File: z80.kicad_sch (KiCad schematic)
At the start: 41 parts, among them IC4 Z80CPU, IC5 LC3664, IC901 TL972

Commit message: more component parts updated
Full in the * as PAL versions.
Added MPN for PCBWAY
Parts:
- C602: MPN (none) -> VJ0805Y104JXJMT
- C901, C902: MPN (none) -> VJ0805V106ZXQTW1BC
- C903: MPN (none) -> VJ0805Y223JXJPW1BC
- C903, C904, C905, C906, C907, C908: MPN (none) -> VJ0805Y105KXJTW1BC
- C910, C911: MPN (none) -> VJ0805A151FXJCW1BC
- IC901: MPN (none) -> TL972IDR
- R901, R902: MPN (none) -> CRCW0805100KFKEA
- R903, R904, R905, R906, R907, R908: MPN (none) -> CRCW0805210KFKEA
- R909, R910: MPN (none) -> CRCW080575R0FKEAHP
- R910, R911: MPN (none) -> RCS0805300KFKEA
- R911: MPN (none) -> CRCW08052K20JNEA
- R912, R913: MPN (none) -> CRCW0805330RFKEA
- R914, R915: MPN (none) -> CRCW080510K0FKEA
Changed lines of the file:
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@@
+      (effects (font (size 1.27 1.27)) hide)
+    )
+    (property "MPN" "VJ0805Y105KXJTW1BC" (at 115.57 231.775 0)
       (effects (font (size 1.27 1.27)) hide)
     )
@@
       (effects (font (size 1.27 1.27)) hide)
     )
+    (property "MPN" "VJ0805A151FXJCW1BC" (at 189.865 175.26 0)
+      (effects (font (size 1.27 1.27)) hide)
+    )
     (pin "1")
     (pin "2")
@@
       (effects (font (size 1.27 1.27)) hide)
     )
+    (property "MPN" "VJ0805V106ZXQTW1BC" (at 115.57 253.365 0)
+      (effects (font (size 1.27 1.27)) hide)
+    )
     (pin "1")
     (pin "2")
@@
     )
     (property "LCSC Part #" "C2080690" (at 145.415 186.055 0)
+      (effects (font (size 1.27 1.27)) hide)
+    )
+    (property "MPN" "CRCW0805210KFKEA" (at 145.415 186.055 0)
       (effects (font (size 1.27 1.27)) hide)
     )
@@
     )
     (property "LCSC Part #" "" (at 221.615 234.315 0)
+      (effects (font (size 1.27 1.27)) hide)
+    )
+    (property "MPN" "" (at 221.615 234.315 0)
       (effects (font (size 1.27 1.27)) hide)
     )
@@
     )
     (property "LCSC Part #" "C46127" (at 189.865 234.315 0)
+      (effects (font (size 1.27 1.27)) hide)
+    )
+    (property "MPN" "TL972IDR" (at 189.865 234.315 0)
       (effects (font (size 1.27 1.27)) hide)
     )
@@
       (effects (font (size 1.27 1.27)) hide)
     )
+    (property "MPN" "CRCW0805210KFKEA" (at 145.415 212.09 0)
+      (effects (font (size 1.27 1.27)) hide)
+    )
     (pin "1")
     (pin "2")
@@
       (effects (font (size 1.27 1.27)) hide)
     )
+    (property "MPN" "CRCW080575R0FKEAHP" (at 101.6 238.76 0)
+      (effects (font (size 1.27 1.27)) hide)
+    )
     (pin "1")
     (pin "2")
@@
     )
     (property "LCSC Part #" "C1850591" (at 115.57 242.57 0)
+      (effects (font (size 1.27 1.27)) hide)
+    )
+    (property "MPN" "VJ0805Y105KXJTW1BC" (at 115.57 242.57 0)
       (effects (font (size 1.27 1.27)) hide)
     )
@@
       (effects (font (size 1.27 1.27)) hide)
     )
+    (property "MPN" "CRCW0805210KFKEA" (at 145.415 231.775 0)
+      (effects (font (size 1.27 1.27)) hide)
+    )
     (pin "1")
     (pin "2")
@@
     )
     (property "LCSC Part #" "C2080690" (at 145.415 242.57 0)
+      (effects (font (size 1.27 1.27)) hide)
+    )
+    (property "MPN" "CRCW0805210KFKEA" (at 145.415 242.57 0)
       (effects (font (size 1.27 1.27)) hide)
     )
@@
       (effects (font (size 1.27 1.27)) hide)
     )
+    (property "MPN" "VJ0805Y104JXJMT" (at 262.89 238.76 0)
+      (effects (font (size 1.27 1.27)) hide)
+    )
     (pin "1")
     (pin "2")
@@
     )
     (property "LCSC Part #" "C844935" (at 145.415 175.26 0)
+      (effects (font (size 1.27 1.27)) hide)
+    )
+    (property "MPN" "CRCW0805100KFKEA" (at 145.415 175.26 0)
       (effects (font (size 1.27 1.27)) hide)
     )
@@
       (effects (font (size 1.27 1.27)) hide)
     )
+    (property "MPN" "CRCW080575R0FKEAHP" (at 52.07 175.26 0)
+      (effects (font (size 1.27 1.27)) hide)
+    )
     (pin "1")
     (pin "2")
@@
     )
     (property "LCSC Part #" "C46127" (at 189.865 194.31 0)
+      (effects (font (size 1.27 1.27)) hide)
+    )
+    (property "MPN" "TL972IDR" (at 189.865 194.31 0)
       (effects (font (size 1.27 1.27)) hide)
     )
@@
       (effects (font (size 1.27 1.27)) hide)
     )
+    (property "MPN" "" (at 80.772 33.782 0)
+      (effects (font (size 1.27 1.27)) hide)
+    )
     (pin "1")
     (pin "2")
@@
       (effects (font (size 1.27 1.27)) hide)
     )
+    (property "MPN" "CRCW0805210KFKEA" (at 145.415 218.44 0)
+      (effects (font (size 1.27 1.27)) hide)
+    )
     (pin "1")
     (pin "2")
@@
       (effects (font (size 1.27 1.27)) hide)
     )
+    (property "MPN" "VJ0805Y223JXJPW1BC" (at 167.64 33.655 0)
+      (effects (font (size 1.27 1.27)) hide)
+    )
     (pin "1")
     (pin "2")
@@
       (effects (font (size 1.27 1.27)) hide)
     )
+    (property "MPN" "VJ0805V106ZXQTW1BC" (at 115.57 175.26 0)
+      (effects (font (size 1.27 1.27)) hide)
+    )
     (pin "1")
     (pin "2")
@@
       (effects (font (size 1.27 1.27)) hide)
     )
+    (property "MPN" "CRCW080510K0FKEA" (at 162.56 222.25 0)
+      (effects (font (size 1.27 1.27)) hide)
+    )
     (pin "1")
     (pin "2")
@@
       (effects (font (size 1.27 1.27)) hide)
     )
+    (property "MPN" "VJ0805Y105KXJTW1BC" (at 115.57 186.055 0)
+      (effects (font (size 1.27 1.27)) hide)
+    )
     (pin "1")
     (pin "2")
@@
       (effects (font (size 1.27 1.27)) hide)
     )
+    (property "MPN" "VJ0805A151FXJCW1BC" (at 189.865 253.365 0)
+      (effects (font (size 1.27 1.27)) hide)
+    )
     (pin "1")
     (pin "2")
@@
       (effects (font (size 1.27 1.27)) hide)
     )
+    (property "MPN" "RCS0805300KFKEA" (at 189.865 186.055 0)
+      (effects (font (size 1.27 1.27)) hide)
+    )
     (pin "1")
     (pin "2")
@@
       (effects (font (size 1.27 1.27)) hide)
     )
+    (property "MPN" "CRCW080510K0FKEA" (at 162.56 208.28 0)
+      (effects (font (size 1.27 1.27)) hide)
+    )
     (pin "1")
     (pin "2")
@@
     )
     (property "LCSC Part #" "C313959" (at 102.235 203.835 0)
+      (effects (font (size 1.27 1.27)) hide)
+    )
+    (property "MPN" "CRCW080575R0FKEAHP" (at 102.235 203.835 0)
       (effects (font (size 1.27 1.27)) hide)
     )
@@
     )
     (property "LCSC Part #" "" (at 221.615 194.31 0)
+      (effects (font (size 1.27 1.27)) hide)
+    )
+    (property "MPN" "" (at 221.615 194.31 0)
       (effects (font (size 1.27 1.27)) hide)
     )
@@
       (effects (font (size 1.27 1.27)) hide)
     )
+    (property "MPN" "" (at 170.18 222.25 0)
+      (effects (font (size 1.27 1.27)) hide)
+    )
     (pin "1")
     (pin "2")
@@
       (effects (font (size 1.27 1.27)) hide)
     )
+    (property "MPN" "VJ0805Y105KXJTW1BC" (at 129.54 218.44 0)
+      (effects (font (size 1.27 1.27)) hide)
+    )
     (pin "1")
     (pin "2")
@@
       (effects (font (size 1.27 1.27)) hide)
     )
+    (property "MPN" "CRCW0805210KFKEA" (at 145.415 196.85 0)
+      (effects (font (size 1.27 1.27)) hide)
+    )
     (pin "1")
     (pin "2")
@@
     )
     (property "LCSC Part #" "C3008897" (at 102.235 222.25 0)
+      (effects (font (size 1.27 1.27)) hide)
+    )
+    (property "MPN" "CRCW08052K20JNEA" (at 102.235 222.25 0)
       (effects (font (size 1.27 1.27)) hide)
     )
@@
       (effects (font (size 1.27 1.27)) hide)
     )
+    (property "MPN" "" (at 275.59 238.76 0)
+      (effects (font (size 1.27 1.27)) hide)
+    )
     (pin "1")
     (pin "2")
@@
       (effects (font (size 1.27 1.27)) hide)
     )
+    (property "MPN" "VJ0805Y223JXJPW1BC" (at 93.472 33.782 0)
+      (effects (font (size 1.27 1.27)) hide)
+    )
     (pin "1")
     (pin "2")
@@
     )
     (property "LCSC Part #" "C844935" (at 145.415 253.365 0)
+      (effects (font (size 1.27 1.27)) hide)
+    )
+    (property "MPN" "CRCW0805100KFKEA" (at 145.415 253.365 0)
       (effects (font (size 1.27 1.27)) hide)
     )
@@
     )
     (property "LCSC Part #" "C844839" (at 210.82 234.315 0)
+      (effects (font (size 1.27 1.27)) hide)
+    )
+    (property "MPN" "CRCW0805330RFKEA" (at 210.82 234.315 0)
       (effects (font (size 1.27 1.27)) hide)
     )
@@
     )
     (property "LCSC Part #" "" (at 74.93 83.185 0)
+      (effects (font (size 1.27 1.27)) hide)
+    )
+    (property "MPN" "" (at 74.93 83.185 0)
       (effects (font (size 1.27 1.27)) hide)
     )
@@
       (effects (font (size 1.27 1.27)) hide)
     )
+    (property "MPN" "TL972IDR" (at 290.195 239.395 0)
+      (effects (font (size 1.27 1.27)) hide)
+    )
     (pin "1")
     (pin "2")
@@
       (effects (font (size 1.27 1.27)) hide)
     )
+    (property "MPN" "RCS0805300KFKEA" (at 189.865 242.57 0)
+      (effects (font (size 1.27 1.27)) hide)
+    )
     (pin "1")
     (pin "2")
@@
     )
     (property "LCSC Part #" "C1850591" (at 129.54 212.09 0)
+      (effects (font (size 1.27 1.27)) hide)
+    )
+    (property "MPN" "VJ0805Y105KXJTW1BC" (at 129.54 212.09 0)
       (effects (font (size 1.27 1.27)) hide)
     )
@@
     )
     (property "LCSC Part #" "C844839" (at 210.82 194.31 0)
+      (effects (font (size 1.27 1.27)) hide)
+    )
+    (property "MPN" "CRCW0805330RFKEA" (at 210.82 194.31 0)
       (effects (font (size 1.27 1.27)) hide)
     )
@@
     )
     (property "LCSC Part #" "" (at 158.75 80.645 0)
+      (effects (font (size 1.27 1.27)) hide)
+    )
+    (property "MPN" "" (at 158.75 80.645 0)
       (effects (font (size 1.27 1.27)) hide)
     )
@@
       (effects (font (size 1.27 1.27)) hide)
     )
+    (property "MPN" "CRCW080575R0FKEAHP" (at 52.07 191.135 0)
+      (effects (font (size 1.27 1.27)) hide)
+    )
     (pin "1")
     (pin "2")
@@
     )
     (property "LCSC Part #" "" (at 219.71 109.22 0)
+      (effects (font (size 1.27 1.27)) hide)
+    )
+    (property "MPN" "" (at 219.71 109.22 0)
       (effects (font (size 1.27 1.27)) hide)
     )
@@
       (effects (font (size 1.27 1.27)) hide)
     )
+    (property "MPN" "VJ0805Y105KXJTW1BC" (at 115.57 196.85 0)
+      (effects (font (size 1.27 1.27)) hide)
+    )

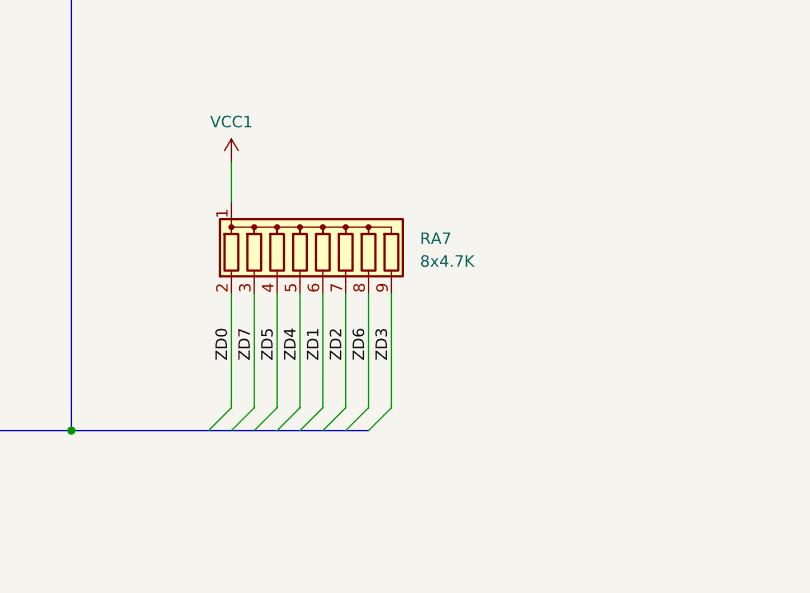
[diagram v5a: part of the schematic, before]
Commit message: Use more readily-available resistor packs.
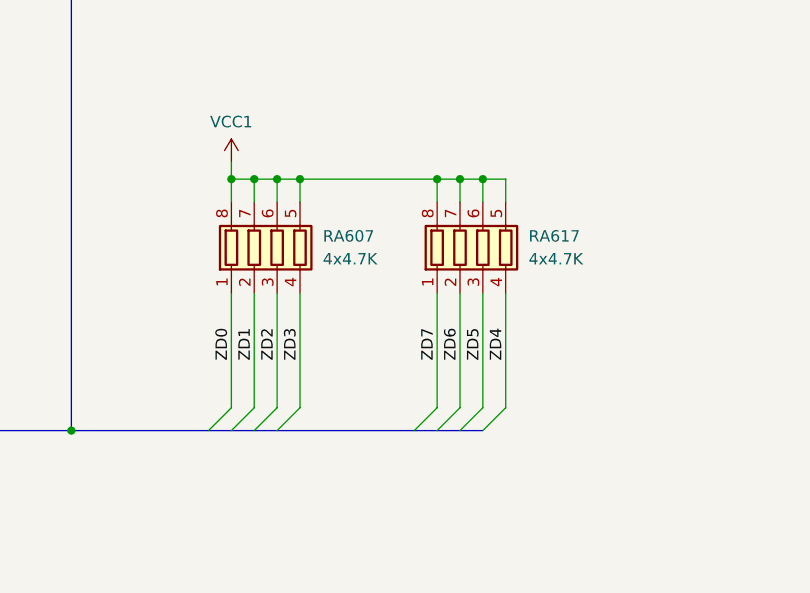
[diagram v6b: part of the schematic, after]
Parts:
- removed RA7: 8x4.7K, Neptune:RA_8_Common, symbol Device:R_Network08
- added RA607, RA617: 4x4.7K, Resistor_SMD:R_Array_Convex_4x0603, symbol Device:R_Pack04
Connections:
- net VCC1: now also RA607.5 (R4.2), RA607.6 (R3.2), RA607.7 (R2.2), RA607.8 (R1.2), RA617.5 (R4.2), RA617.6 (R3.2), RA617.7 (R2.2), RA617.8 (R1.2)
- net ZD0: now also RA607.1 (R1.1)
- net ZD1: now also RA607.2 (R2.1)
- net ZD2: now also RA607.3 (R3.1)
- net ZD3: now also RA607.4 (R4.1)
- net ZD4: now also RA617.4 (R4.1)
- net ZD5: now also RA617.3 (R3.1)
- net ZD6: now also RA617.2 (R2.1)
- net ZD7: now also RA617.1 (R1.1)

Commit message: Added resistor array parts
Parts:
- RA607, RA617: LCSC Part # (none) -> C700514; MPN (none) -> YC164-FR-074K7L
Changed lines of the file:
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@@
+      (effects (font (size 1.27 1.27)) hide)
+    )
+    (property "LCSC Part #" "C700514" (at 214.63 109.22 0)
+      (effects (font (size 1.27 1.27)) hide)
+    )
+    (property "MPN" "YC164-FR-074K7L" (at 214.63 109.22 0)
       (effects (font (size 1.27 1.27)) hide)
     )
@@
       (effects (font (size 1.27 1.27)) hide)
     )
+    (property "LCSC Part #" "C700514" (at 237.49 109.22 0)
+      (effects (font (size 1.27 1.27)) hide)
+    )
+    (property "MPN" "YC164-FR-074K7L" (at 237.49 109.22 0)
+      (effects (font (size 1.27 1.27)) hide)
+    )

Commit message: Update LCSC parts
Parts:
- C602: LCSC Part # C2237864 -> C111492
- C901, C902: LCSC Part # C2265547 -> C89832
- C903: LCSC Part # C2224419 -> C520037
- C903, C904, C905, C906, C907, C908: LCSC Part # C1850591 -> C94122
- C910, C911: LCSC Part # C2230620 -> C107111
- R903, R904, R905, R906, R907, R908: LCSC Part # C2080690 -> C228629
- R909, R910: LCSC Part # C313959 -> C136912
- R910, R911: LCSC Part # C1881308 -> C865386
- R911: LCSC Part # C3008897 -> C114561
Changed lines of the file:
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@@
       (effects (font (size 1.27 1.27)) hide)
     )
-    (property "LCSC Part #" "C1850591" (at 115.57 231.775 0)
+    (property "LCSC Part #" "C94122" (at 115.57 231.775 0)
       (effects (font (size 1.27 1.27)) hide)
     )
@@
       (effects (font (size 1.27 1.27)) hide)
     )
-    (property "LCSC Part #" "C2230620" (at 189.865 175.26 0)
+    (property "LCSC Part #" "C107111" (at 189.865 175.26 0)
       (effects (font (size 1.27 1.27)) hide)
     )
@@
       (effects (font (size 1.27 1.27)) hide)
     )
-    (property "LCSC Part #" "C2265547" (at 115.57 253.365 0)
+    (property "LCSC Part #" "C89832" (at 115.57 253.365 0)
       (effects (font (size 1.27 1.27)) hide)
     )
@@
       (effects (font (size 1.27 1.27)) hide)
     )
-    (property "LCSC Part #" "C2080690" (at 145.415 186.055 0)
+    (property "LCSC Part #" "C228629" (at 145.415 186.055 0)
       (effects (font (size 1.27 1.27)) hide)
     )
@@
       (effects (font (size 1.27 1.27)) hide)
     )
-    (property "LCSC Part #" "C2080690" (at 145.415 212.09 0)
+    (property "LCSC Part #" "C228629" (at 145.415 212.09 0)
       (effects (font (size 1.27 1.27)) hide)
     )
@@
       (effects (font (size 1.27 1.27)) hide)
     )
-    (property "LCSC Part #" "C313959" (at 101.6 238.76 0)
+    (property "LCSC Part #" "C136912" (at 101.6 238.76 0)
       (effects (font (size 1.27 1.27)) hide)
     )
@@
       (effects (font (size 1.27 1.27)) hide)
     )
-    (property "LCSC Part #" "C1850591" (at 115.57 242.57 0)
+    (property "LCSC Part #" "C94122" (at 115.57 242.57 0)
       (effects (font (size 1.27 1.27)) hide)
     )
@@
       (effects (font (size 1.27 1.27)) hide)
     )
-    (property "LCSC Part #" "C2080690" (at 145.415 231.775 0)
+    (property "LCSC Part #" "C228629" (at 145.415 231.775 0)
       (effects (font (size 1.27 1.27)) hide)
     )
@@
       (effects (font (size 1.27 1.27)) hide)
     )
-    (property "LCSC Part #" "C2080690" (at 145.415 242.57 0)
+    (property "LCSC Part #" "C228629" (at 145.415 242.57 0)
       (effects (font (size 1.27 1.27)) hide)
     )
@@
       (effects (font (size 1.27 1.27)) hide)
     )
-    (property "LCSC Part #" "C2237864" (at 262.89 238.76 0)
+    (property "LCSC Part #" "C111492" (at 262.89 238.76 0)
       (effects (font (size 1.27 1.27)) hide)
     )
@@
       (effects (font (size 1.27 1.27)) hide)
     )
-    (property "LCSC Part #" "C313959" (at 52.07 175.26 0)
+    (property "LCSC Part #" "C136912" (at 52.07 175.26 0)
       (effects (font (size 1.27 1.27)) hide)
     )
@@
       (effects (font (size 1.27 1.27)) hide)
     )
-    (property "LCSC Part #" "C2080690" (at 145.415 218.44 0)
+    (property "LCSC Part #" "C228629" (at 145.415 218.44 0)
       (effects (font (size 1.27 1.27)) hide)
     )
@@
       (effects (font (size 1.27 1.27)) hide)
     )
-    (property "LCSC Part #" "C2224419" (at 167.64 33.655 0)
+    (property "LCSC Part #" "C520037" (at 167.64 33.655 0)
       (effects (font (size 1.27 1.27)) hide)
     )
@@
       (effects (font (size 1.27 1.27)) hide)
     )
-    (property "LCSC Part #" "C2265547" (at 115.57 175.26 0)
+    (property "LCSC Part #" "C89832" (at 115.57 175.26 0)
       (effects (font (size 1.27 1.27)) hide)
     )
@@
       (effects (font (size 1.27 1.27)) hide)
     )
-    (property "LCSC Part #" "C1850591" (at 115.57 186.055 0)
+    (property "LCSC Part #" "C94122" (at 115.57 186.055 0)
       (effects (font (size 1.27 1.27)) hide)
     )
@@
       (effects (font (size 1.27 1.27)) hide)
     )
-    (property "LCSC Part #" "C2230620" (at 189.865 253.365 0)
+    (property "LCSC Part #" "C107111" (at 189.865 253.365 0)
       (effects (font (size 1.27 1.27)) hide)
     )
@@
       (effects (font (size 1.27 1.27)) hide)
     )
-    (property "LCSC Part #" "C1881308" (at 189.865 186.055 0)
+    (property "LCSC Part #" "C865386" (at 189.865 186.055 0)
       (effects (font (size 1.27 1.27)) hide)
     )
@@
       (effects (font (size 1.27 1.27)) hide)
     )
-    (property "LCSC Part #" "C313959" (at 102.235 203.835 0)
+    (property "LCSC Part #" "C136912" (at 102.235 203.835 0)
       (effects (font (size 1.27 1.27)) hide)
     )
@@
       (effects (font (size 1.27 1.27)) hide)
     )
-    (property "LCSC Part #" "C1850591" (at 129.54 218.44 0)
+    (property "LCSC Part #" "C94122" (at 129.54 218.44 0)
       (effects (font (size 1.27 1.27)) hide)
     )
@@
       (effects (font (size 1.27 1.27)) hide)
     )
-    (property "LCSC Part #" "C2080690" (at 145.415 196.85 0)
+    (property "LCSC Part #" "C228629" (at 145.415 196.85 0)
       (effects (font (size 1.27 1.27)) hide)
     )
@@
       (effects (font (size 1.27 1.27)) hide)
     )
-    (property "LCSC Part #" "C3008897" (at 102.235 222.25 0)
+    (property "LCSC Part #" "C114561" (at 102.235 222.25 0)
       (effects (font (size 1.27 1.27)) hide)
     )
@@
       (effects (font (size 1.27 1.27)) hide)
     )
-    (property "LCSC Part #" "C2224419" (at 93.472 33.782 0)
+    (property "LCSC Part #" "C520037" (at 93.472 33.782 0)
       (effects (font (size 1.27 1.27)) hide)
     )
@@
       (effects (font (size 1.27 1.27)) hide)
     )
-    (property "LCSC Part #" "C1881308" (at 189.865 242.57 0)
+    (property "LCSC Part #" "C865386" (at 189.865 242.57 0)
       (effects (font (size 1.27 1.27)) hide)
     )
@@
       (effects (font (size 1.27 1.27)) hide)
     )
-    (property "LCSC Part #" "C1850591" (at 129.54 212.09 0)
+    (property "LCSC Part #" "C94122" (at 129.54 212.09 0)
       (effects (font (size 1.27 1.27)) hide)
     )
@@
       (effects (font (size 1.27 1.27)) hide)
     )
-    (property "LCSC Part #" "C313959" (at 52.07 191.135 0)
+    (property "LCSC Part #" "C136912" (at 52.07 191.135 0)
       (effects (font (size 1.27 1.27)) hide)
     )
@@
       (effects (font (size 1.27 1.27)) hide)
     )
-    (property "LCSC Part #" "C1850591" (at 115.57 196.85 0)
-      (effects (font (size 1.27 1.27)) hide)
-    )
+    (property "LCSC Part #" "C94122" (at 115.57 196.85 0)
+      (effects (font (size 1.27 1.27)) hide)
+    )
